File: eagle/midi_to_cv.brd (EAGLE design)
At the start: 100 x 80 mm, 76 parts, among them IC1 TL084P, IC2 TL084P, IC3 TL084P, IC4 TL084P, IC5 TL084P, U1 ATMEGA328P_PDIP

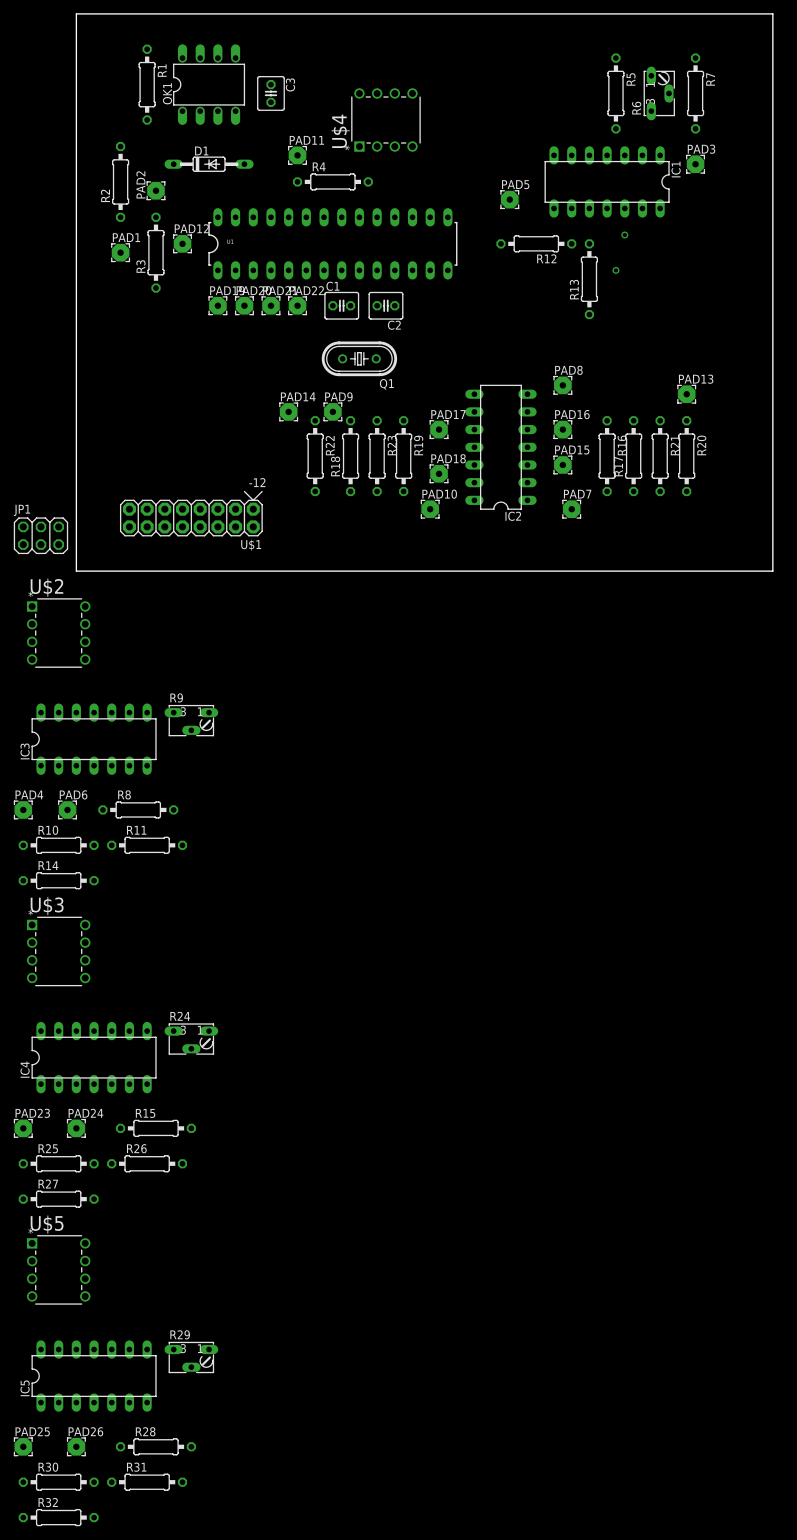
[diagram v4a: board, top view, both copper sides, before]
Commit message: renumbered op amps
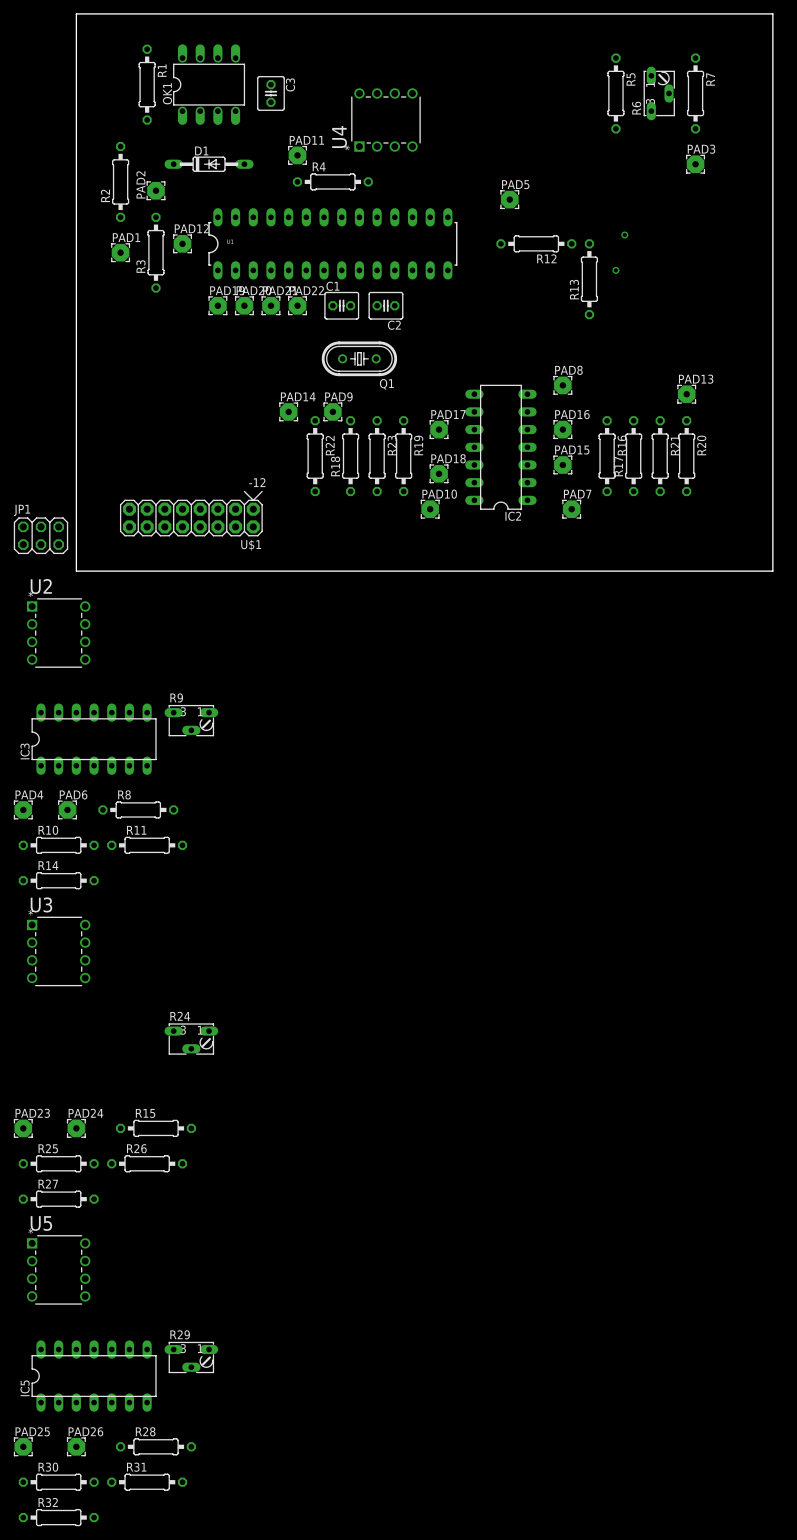
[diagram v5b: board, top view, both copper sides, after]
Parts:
- removed IC1, IC4: TL084P, linear:DIL14
- renumbered U$2 to U2, U$3 to U3, U$4 to U4, U$5 to U5
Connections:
- net +12V: no longer IC1.4, IC4.4
- net -12V: no longer IC1.11, IC4.11
- net N$12: now also IC5.6; no longer IC1.2
- net N$19: now also IC5.14; no longer IC1.8
- net N$20: now also IC5.13; no longer IC1.9
- net N$26: now also IC3.5; no longer IC4.3
- net N$49: now also IC3.7; no longer IC4.1
- net N$50: now also IC3.6; no longer IC4.2
- net N$51: now also IC5.12; no longer IC1.10
- net N$52: now also IC3.14; no longer IC4.8
- net N$53: now also IC3.13; no longer IC4.9
- net N$54: now also IC3.12; no longer IC4.10
- net N$6: now also IC5.5; no longer IC1.3
- net N$9: now also IC5.7; no longer IC1.1

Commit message: moved parts onto board area
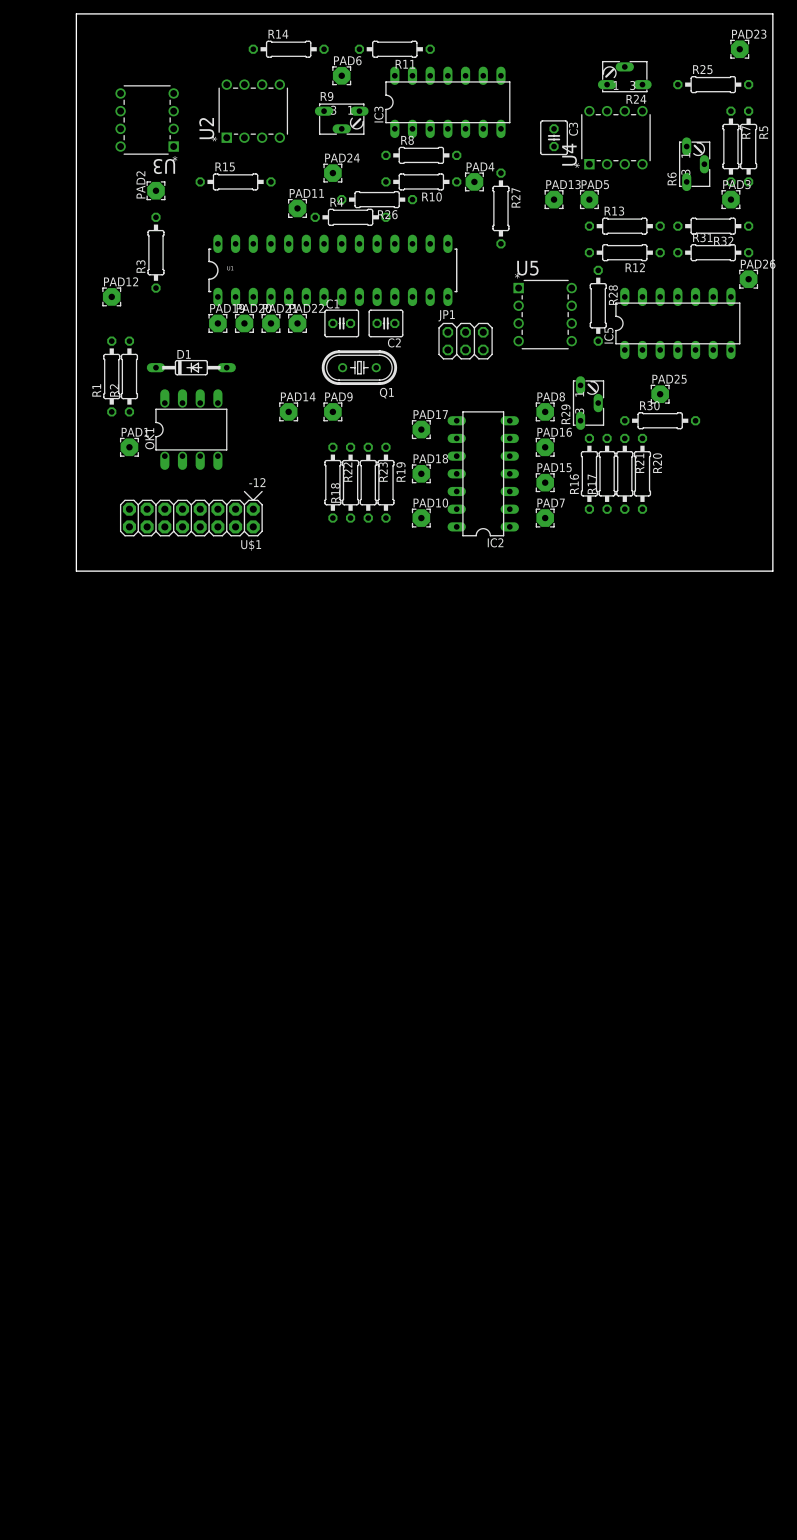
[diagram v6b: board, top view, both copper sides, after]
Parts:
- moved R32 207.9 mm to (91.4, 49.5), turned to 180 degrees
- moved R31 194.3 mm to (91.4, 45.7)
- moved PAD26 193.4 mm to (96.5, 41.9)
- moved PAD23 186.0 mm to (95.2, 74.9)
- moved R25 181.2 mm to (91.4, 69.8)
- moved PAD25 176.6 mm to (83.8, 25.4)
- moved R28 175.7 mm to (74.9, 38.1), turned to 270 degrees
- moved R30 175.2 mm to (83.8, 21.6)
- moved IC5 172.8 mm to (86.4, 35.6)
- moved R27 155.8 mm to (61.0, 52.1), turned to 270 degrees
- moved U5 153.9 mm to (71.1, 33.0)
- moved R24 149.5 mm to (78.7, 69.8), turned to 180 degrees
- moved R29 146.9 mm to (72.4, 24.1), turned to 90 degrees
- moved R26 142.3 mm to (43.2, 53.3), turned to 180 degrees
- moved PAD24 142.0 mm to (36.8, 57.1)
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
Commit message: working to route the board
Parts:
- removed IC3, IC5: TL084P, linear:DIL14
- removed JP1: (no value), pinhead:2X03
- added IC1, IC4, IC6, IC7: TL082P, linear:DIL08
- moved R25 78.8 mm to (12.7, 72.4)
- moved PAD23 72.4 mm to (22.9, 73.7)
- moved R24 63.8 mm to (15.2, 63.5), turned to 270 degrees
- moved C3 54.6 mm to (19.1, 39.4), turned to 90 degrees
- moved PAD2 42.0 mm to (29.2, 16.5)
- moved R32 35.8 mm to (57.1, 59.7), turned to 270 degrees
- moved R14 33.1 mm to (63.5, 72.4), turned to 180 degrees
- moved PAD19 32.2 mm to (52.1, 30.5)
- moved R27 31.2 mm to (33.0, 66.0)
- moved R5 29.2 mm to (67.3, 61.0), turned to 0 degrees
- moved PAD4 22.6 mm to (43.2, 73.7)
- moved R6 21.7 mm to (67.3, 66.0), turned to 180 degrees
- moved U4 21.1 mm to (69.8, 48.3), turned to 0 degrees
- moved R31 20.9 mm to (86.4, 25.4)
- moved PAD13 19.4 mm to (72.4, 72.4)
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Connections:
- net +12V: now also IC1.8, IC4.8, IC6.8, IC7.8; no longer IC3.4, IC5.4
- net -12V: now also IC1.4, IC4.4, IC6.4, IC7.4; no longer IC3.11, IC5.11
- net N$12: now also IC7.2; no longer IC5.6
- net N$16: now also IC1.3; no longer IC3.3
- net N$17: now also IC1.1; no longer IC3.1
- net N$18: now also IC1.2; no longer IC3.2
- net N$19: now also IC7.7; no longer IC5.14
- net N$20: now also IC7.6; no longer IC5.13
- net N$21: now also IC1.7; no longer IC3.8
- net N$22: now also IC1.6; no longer IC3.9
- net N$24: now also IC1.5; no longer IC3.10
- net N$26: now also IC4.3; no longer IC3.5
- net N$49: now also IC4.1; no longer IC3.7
- net N$50: now also IC4.2; no longer IC3.6
- net N$51: now also IC7.5; no longer IC5.12
- net N$52: now also IC4.7; no longer IC3.14
- net N$53: now also IC4.6; no longer IC3.13
- net N$54: now also IC4.5; no longer IC3.12
- net N$56: now also IC6.3; no longer IC5.3
- net N$57: now also IC6.1; no longer IC5.1
- net N$58: now also IC6.2; no longer IC5.2
- net N$59: now also IC6.7; no longer IC5.8
- net N$6: now also IC7.3; no longer IC5.5
- net N$60: now also IC6.6; no longer IC5.9
- net N$61: now also IC6.5; no longer IC5.10
- net N$9: now also IC7.1; no longer IC5.7

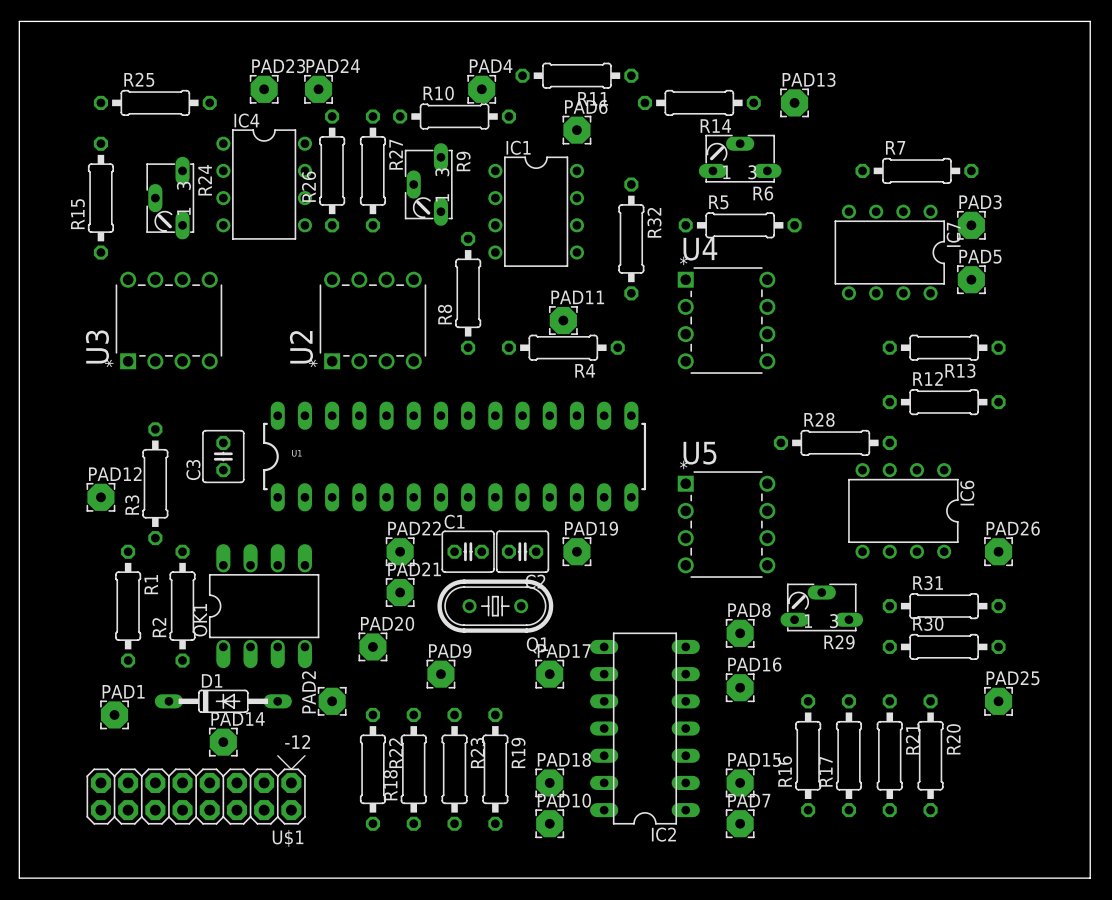
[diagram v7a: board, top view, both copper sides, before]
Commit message: swapped dac control lines and need to do so in software
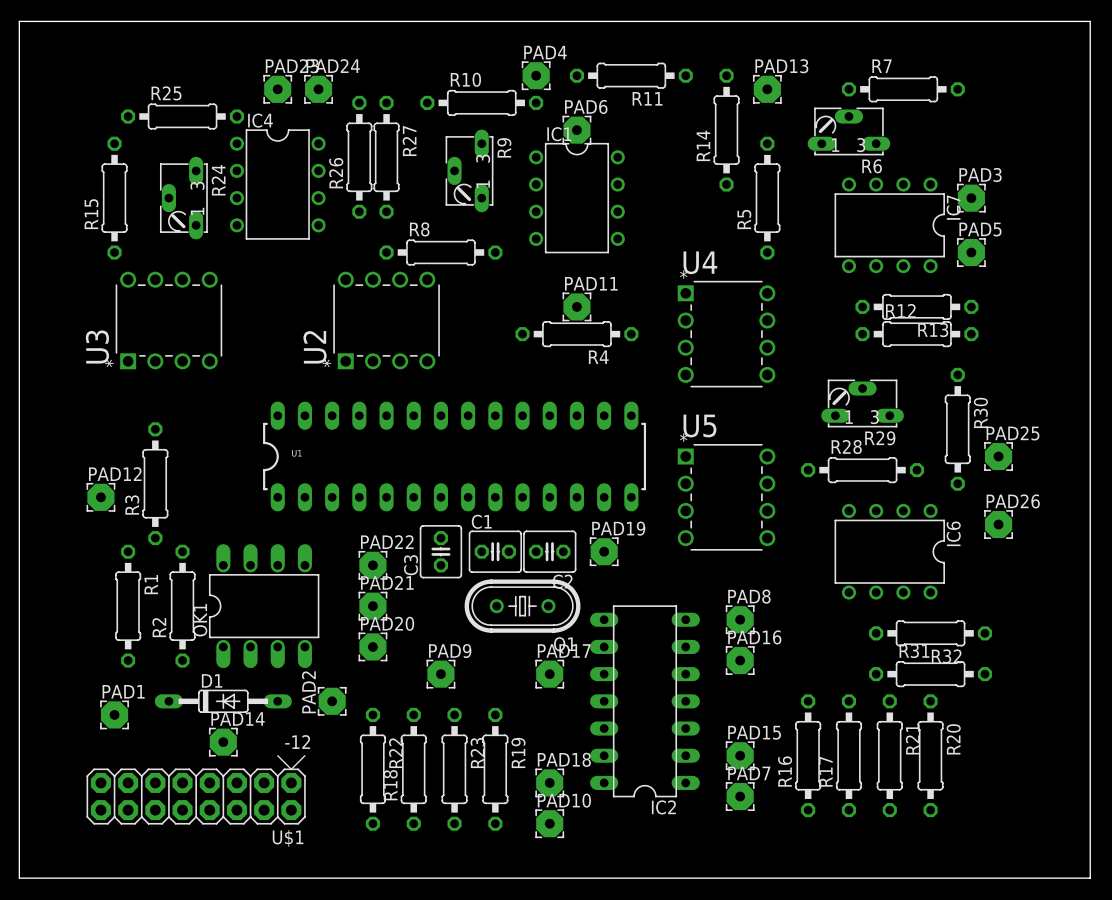
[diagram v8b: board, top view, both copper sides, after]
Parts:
- moved R32 46.2 mm to (85.1, 22.9), turned to 180 degrees
- moved PAD25 22.9 mm to (91.4, 39.4)
- moved C3 22.2 mm to (39.4, 30.5)
- moved R30 20.4 mm to (87.6, 41.9), turned to 270 degrees
- moved R29 19.4 mm to (78.7, 43.2)
- moved R6 10.5 mm to (77.5, 68.6)
- moved R7 7.73 mm to (82.5, 73.7)
- moved R12 6.84 mm to (83.8, 50.8)
- moved R31 6.48 mm to (85.1, 19.1)
- moved PAD4 5.24 mm to (48.3, 74.9)
- moved R11 5.08 mm to (57.1, 74.9)
- moved R13 4.58 mm to (83.8, 53.3)
- moved R8 4.58 mm to (39.4, 58.4), turned to 0 degrees
- moved R9 4.02 mm to (43.2, 66.0)
- moved IC1 4.02 mm to (52.1, 63.5)
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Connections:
- removed net N$23: U1.14, U5.4
- new net N$68: U1.14, U5.3
- net N$14: now also U4.3; no longer U4.4
- net N$15: now also U4.4; no longer U4.3
- net N$28: now also U5.4; no longer U5.3
- net N$62: now also U2.4; no longer U2.3
- net N$63: now also U2.3; no longer U2.4
- net N$65: now also U3.4; no longer U3.3
- net N$66: now also U3.3; no longer U3.4
